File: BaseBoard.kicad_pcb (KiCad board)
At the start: 2 copper layers, 225 x 225 mm, 154 parts, among them Q1 MMBT2222A-7-F, Q10 IRLML6401TRPBF, Q11 MMBT2222A-7-F, Q12 IRLML6401TRPBF, Q13 MMBT2222A-7-F, Q14 IRLML6401TRPBF, Q15 MMBT2222A-7-F, Q16 IRLML6401TRPBF, Q2 IRLML6401TRPBF, Q3 MMBT2222A-7-F, Q4 IRLML6401TRPBF, Q5 MMBT2222A-7-F, Q6 IRLML6401TRPBF, Q7 MMBT2222A-7-F, Q8 IRLML6401TRPBF, Q9 MMBT2222A-7-F, U1 TLC5971PWPR, U10 TLC5971PWPR, U11 TLC5971PWPR, U12 TLC5971PWPR, U13 TLC5971PWPR, U14 TLC5971PWPR, U15 TLC5971PWPR, U16 TLC5971PWPR, U2 TLC5971PWPR, U3 TLC5971PWPR, U4 TLC5971PWPR, U5 TLC5971PWPR, U6 TLC5971PWPR, U7 TLC5971PWPR, U8 TLC5971PWPR, U9 TLC5971PWPR

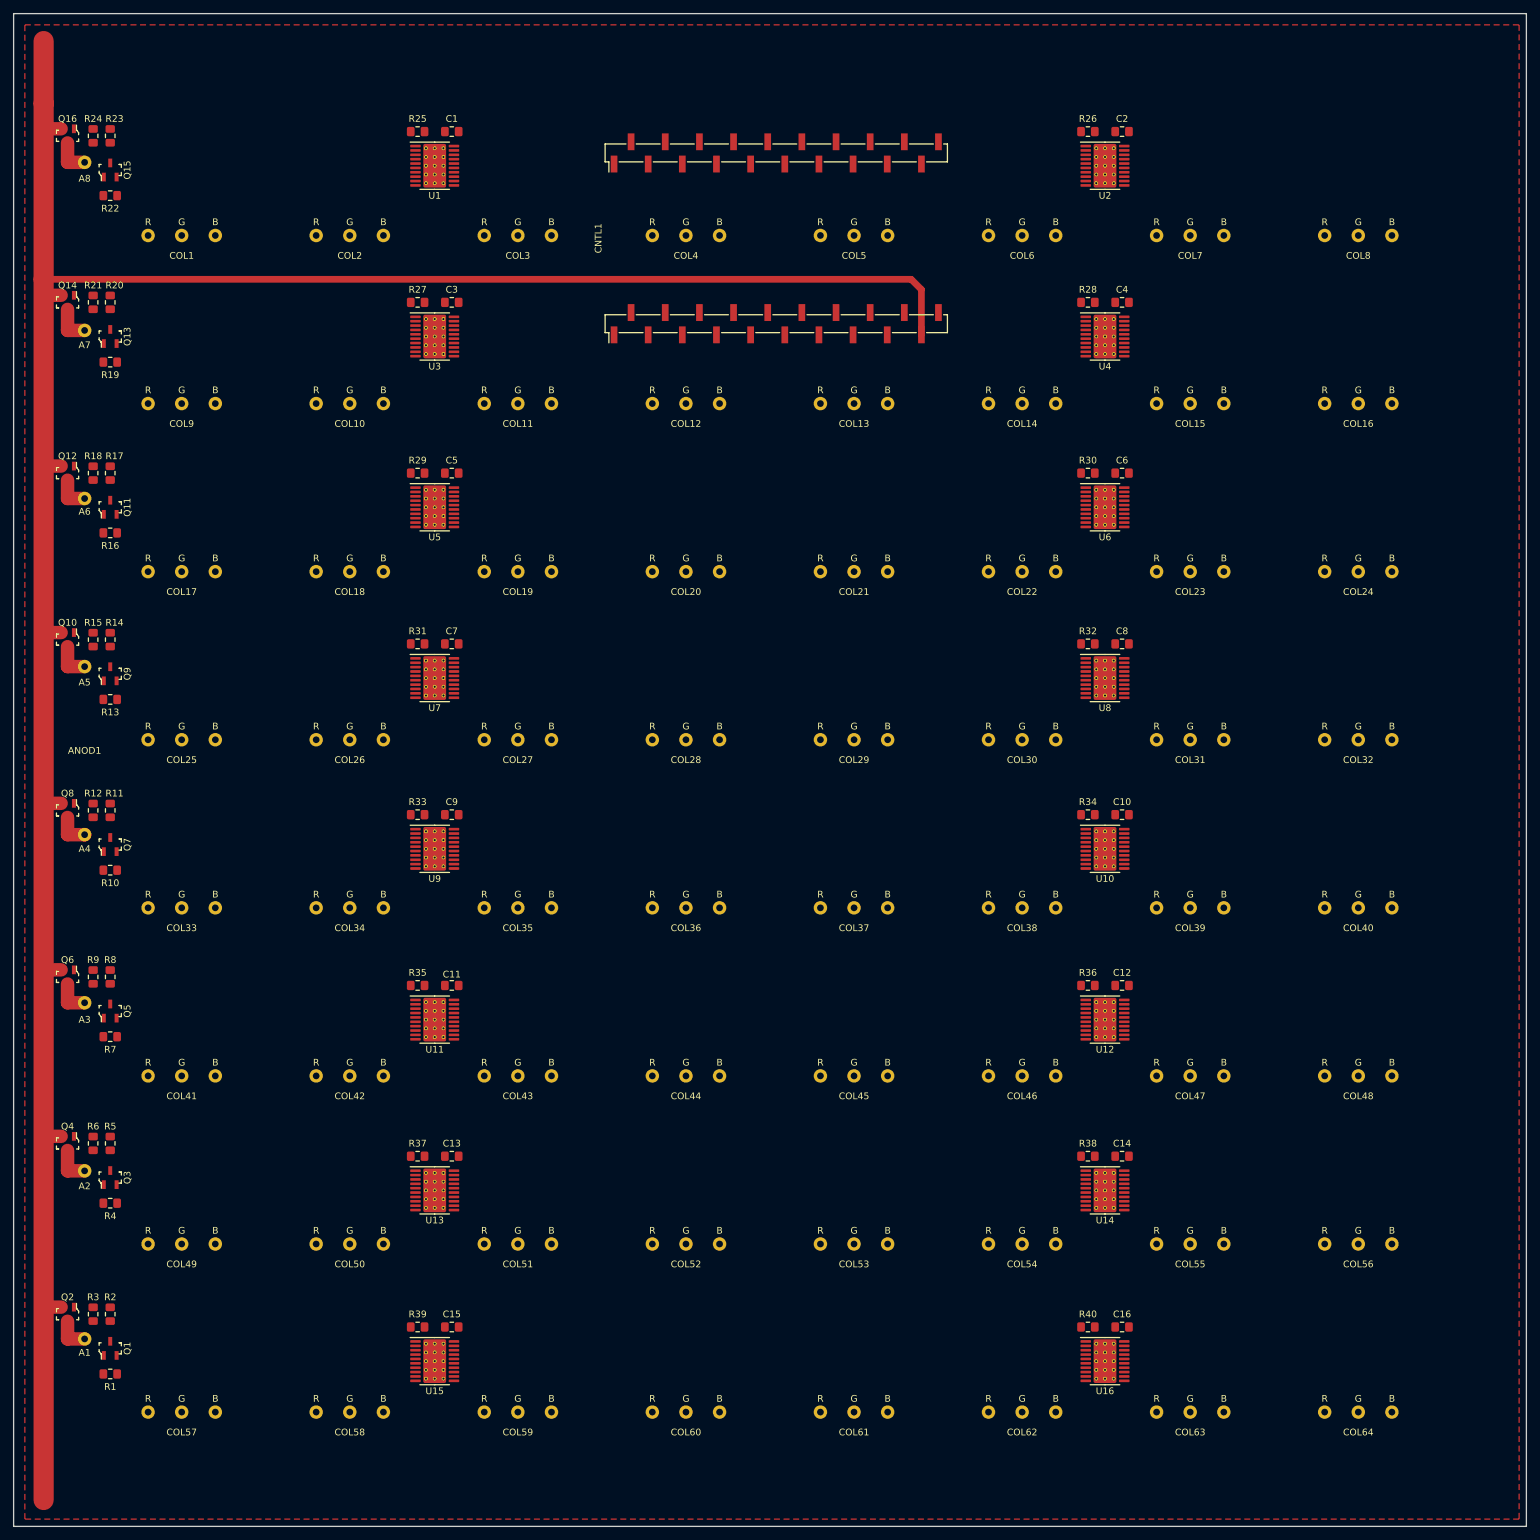
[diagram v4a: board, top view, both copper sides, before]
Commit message: Realign some components
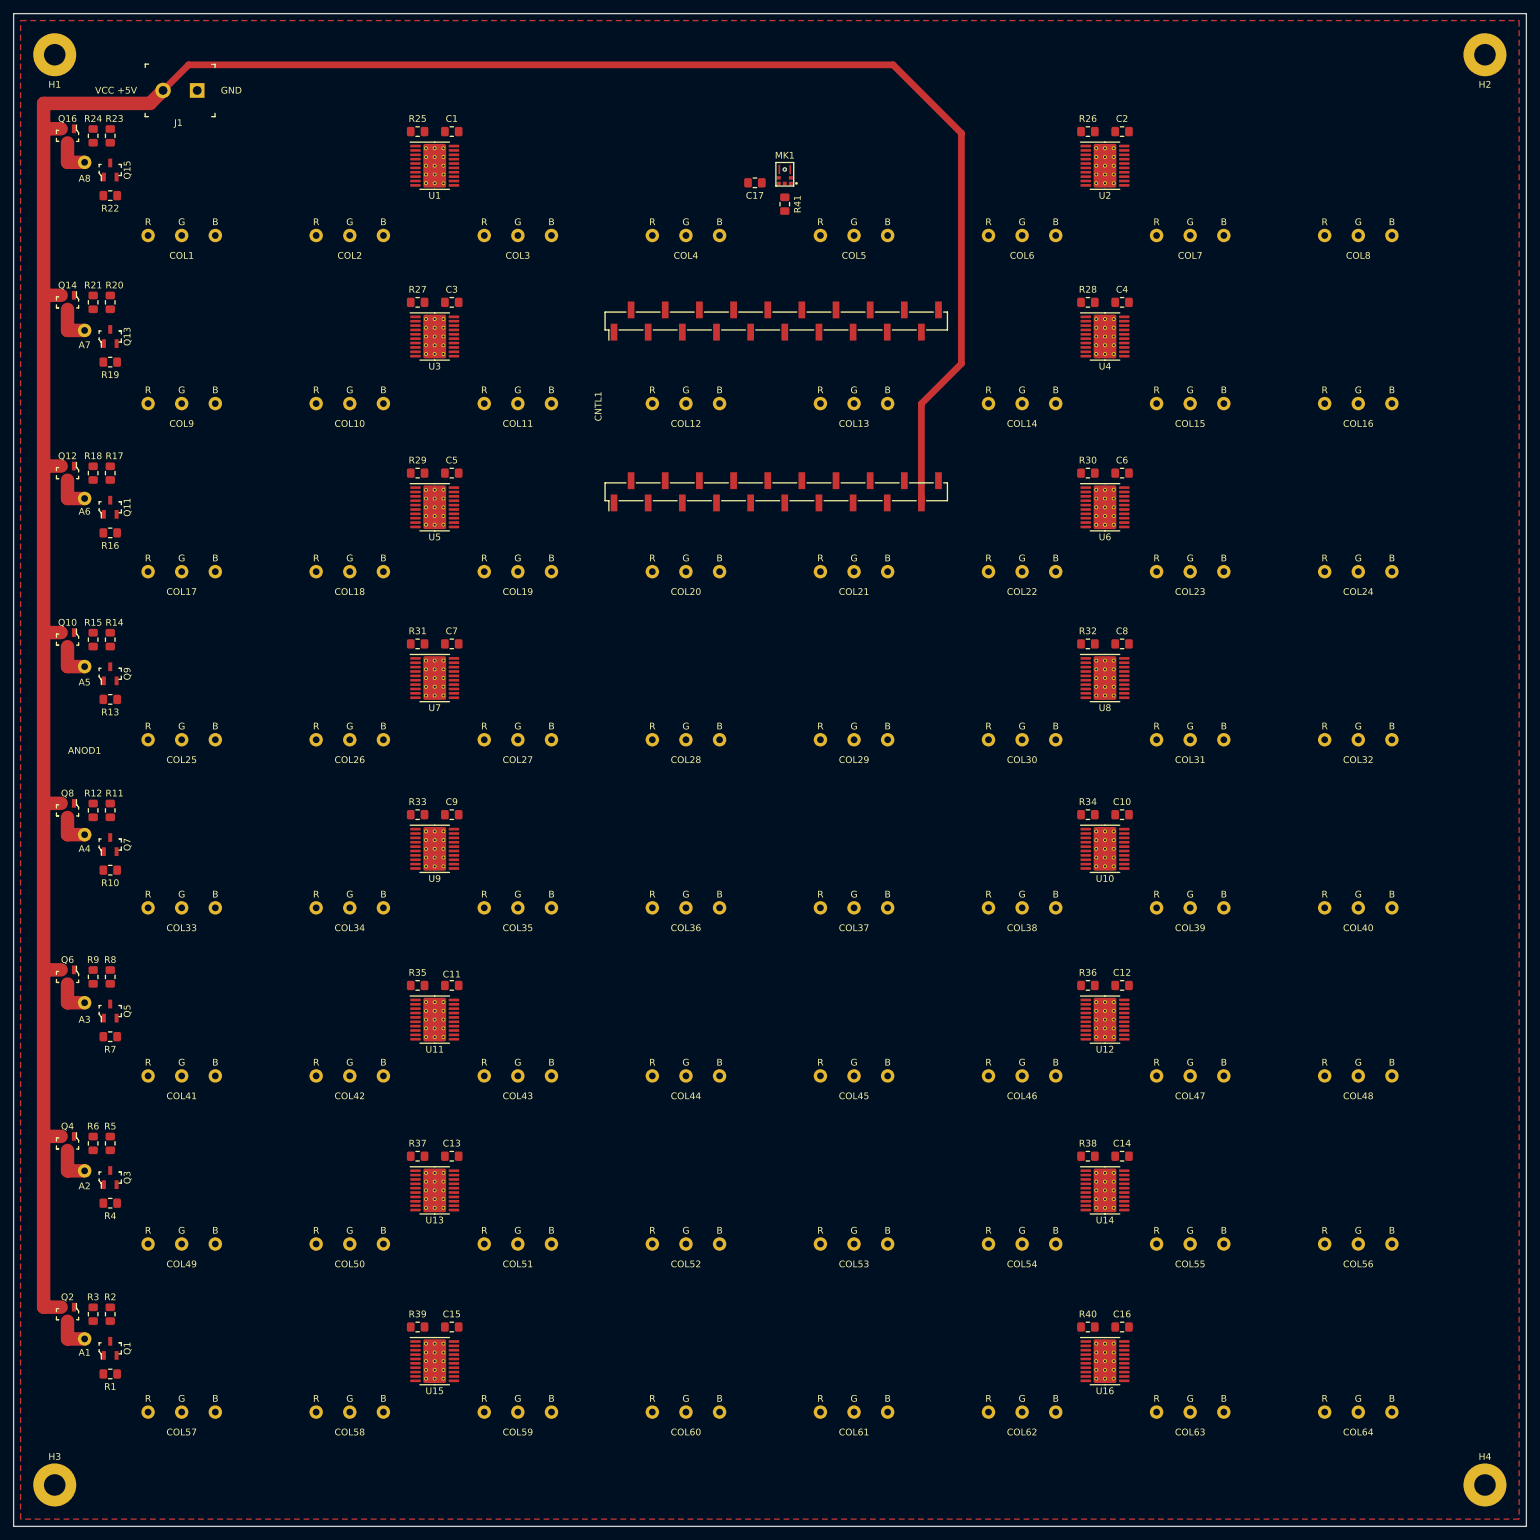
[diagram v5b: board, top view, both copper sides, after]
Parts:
- added C17: 0.1uF, Capacitor_SMD:C_0805_2012Metric_Pad1.15x1.40mm_HandSolder, F.Cu at (130.2, 45.1)
- added H1: MountingHole_3.2mm_M3_Pad, MountingHole:MountingHole_3.2mm_M3_Pad, F.Cu at (26.0, 26.0)
- added H2: MountingHole_3.2mm_M3_Pad, MountingHole:MountingHole_3.2mm_M3_Pad, F.Cu at (238.8, 26.0)
- added H3: MountingHole_3.2mm_M3_Pad, MountingHole:MountingHole_3.2mm_M3_Pad, F.Cu at (26.0, 238.8)
- added H4: MountingHole_3.2mm_M3_Pad, MountingHole:MountingHole_3.2mm_M3_Pad, F.Cu at (238.8, 238.8)
- added J1: OSTTC022162, digikey-footprints:Term_Block_1x2_P5.08MM, F.Cu at (47.2, 31.4)
- added MK1: ICS-43434, BaseBoard:MIC_ICS-43434, F.Cu at (134.6, 43.8)
- added R41: 100K, Resistor_SMD:R_0805_2012Metric_Pad1.15x1.40mm_HandSolder, F.Cu at (134.6, 48.3)
- moved CNTL1 25.0 mm to (133.3, 78.3)
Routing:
- net VCC: track 375.7 -> 400.4 mm
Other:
- board text added: "GND"
- board text added: "VCC +5V"

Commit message: Add all routing
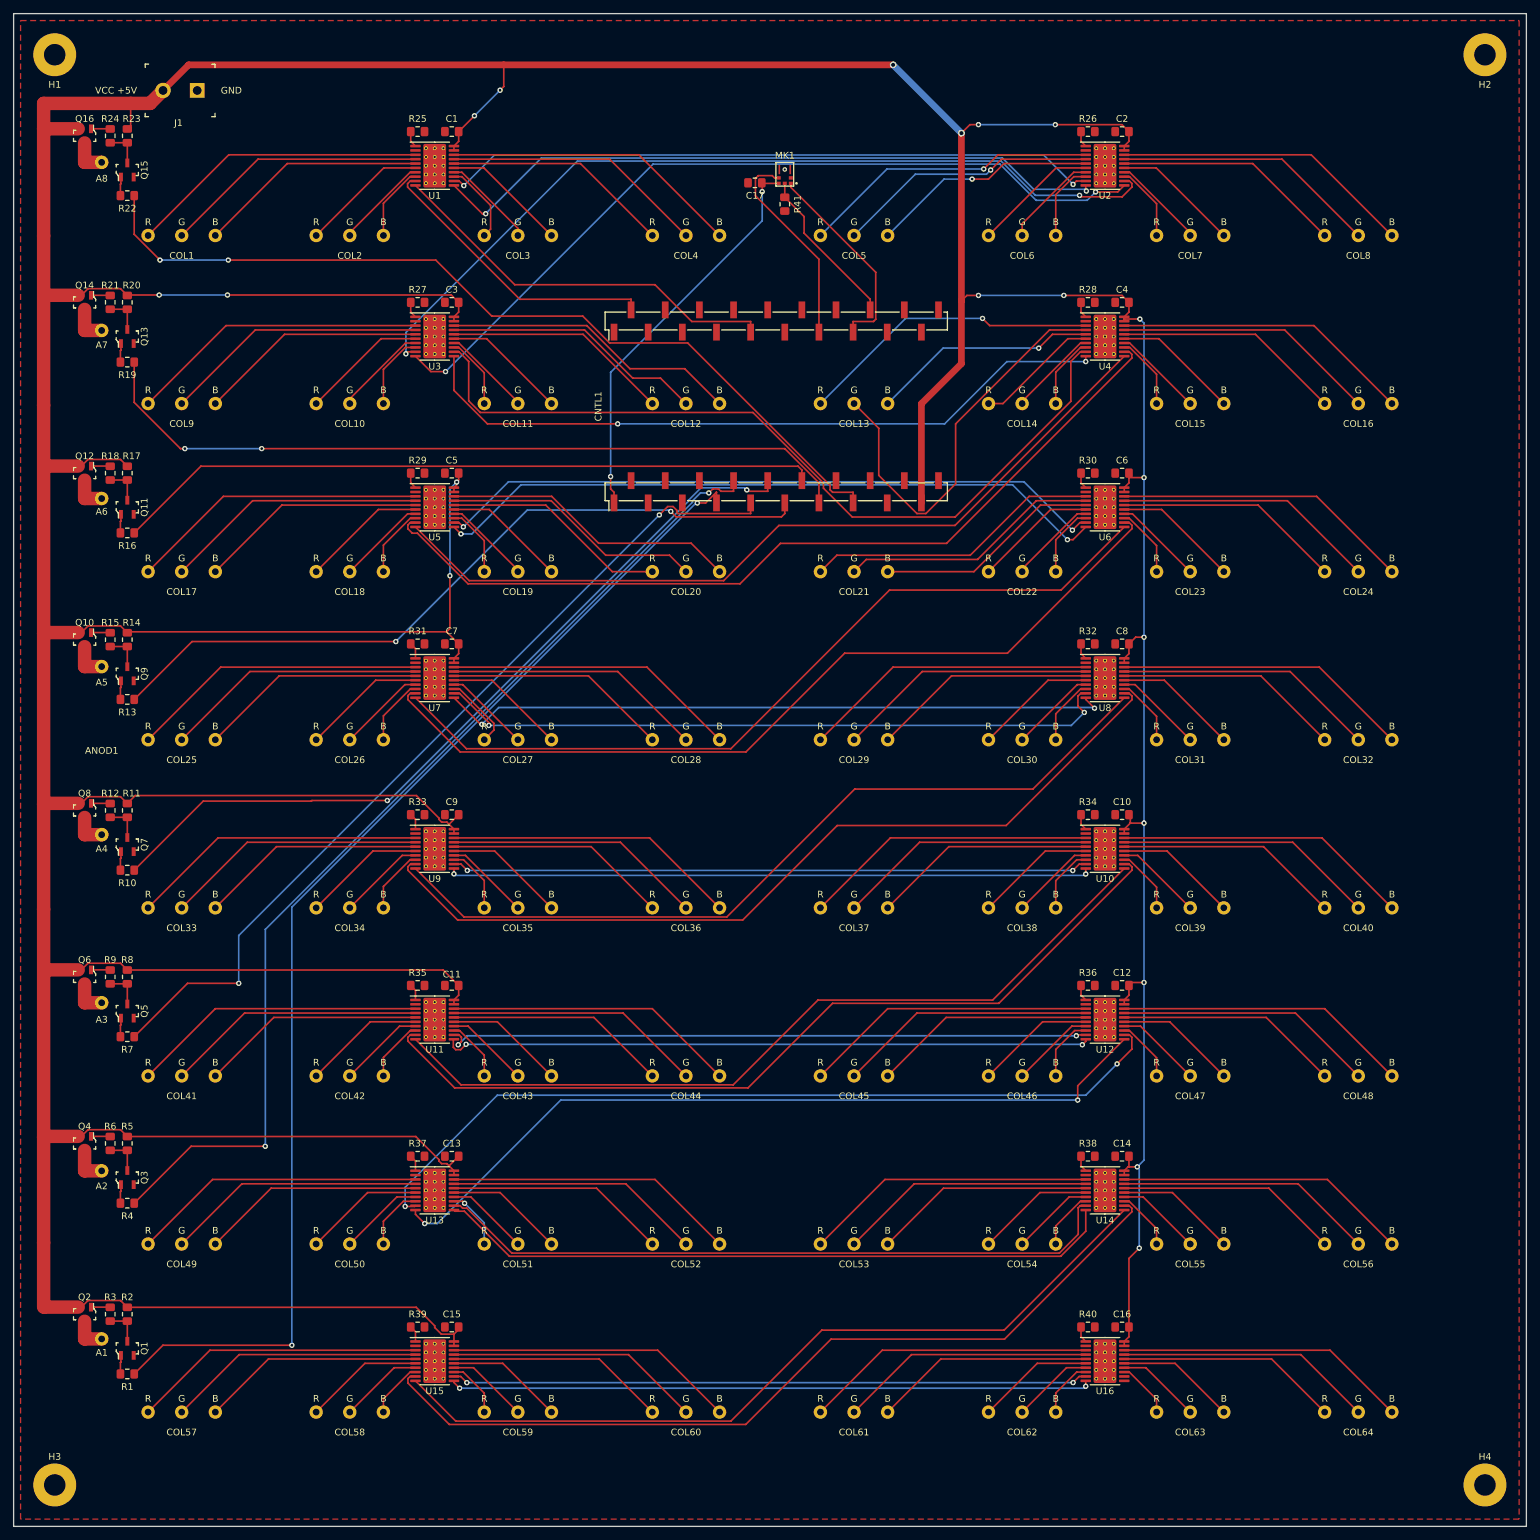
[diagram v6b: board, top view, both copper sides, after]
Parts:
- moved ANOD1 2.54 mm to (33.0, 129.5)
- moved Q1 2.54 mm to (36.8, 218.4)
- moved Q10 2.54 mm to (30.5, 113.0)
- moved Q11 2.54 mm to (36.8, 93.3)
- moved Q12 2.54 mm to (30.5, 88.3)
- moved Q13 2.54 mm to (36.8, 67.9)
- moved Q14 2.54 mm to (30.5, 62.9)
- moved Q15 2.54 mm to (36.8, 43.2)
- moved Q16 2.54 mm to (30.5, 38.1)
- moved Q2 2.54 mm to (30.5, 213.4)
- moved Q3 2.54 mm to (36.8, 193.0)
- moved Q4 2.54 mm to (30.5, 188.0)
- moved Q5 2.54 mm to (36.8, 168.3)
- moved Q6 2.54 mm to (30.5, 163.2)
- moved Q7 2.54 mm to (36.8, 143.5)
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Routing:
- net VCC: track 400.4 -> 1121.5 mm, vias 0 -> 19
- net Net-(CNTL1-Pad7): track 0.00 -> 180.7 mm, vias 0 -> 2
- net Net-(CNTL1-Pad8): track 0.00 -> 153.9 mm, vias 0 -> 2
- net Net-(CNTL1-Pad9): track 0.00 -> 130.7 mm, vias 0 -> 2
- net Net-(CNTL1-Pad15): track 0.00 -> 130.5 mm, vias 0 -> 2
- net Net-(U4-Pad12): track 0.00 -> 128.6 mm
- net Net-(U6-Pad12): track 0.00 -> 128.3 mm
- net Net-(U8-Pad12): track 0.00 -> 128.0 mm
- net Net-(U2-Pad12): track 0.00 -> 127.9 mm, vias 0 -> 2
- net Net-(U10-Pad12): track 0.00 -> 127.7 mm
- net Net-(U14-Pad12): track 0.00 -> 127.1 mm
- net Net-(U12-Pad12): track 0.00 -> 124.1 mm, vias 0 -> 2
- net Net-(U4-Pad11): track 0.00 -> 122.6 mm
- net Net-(U2-Pad11): track 0.00 -> 122.3 mm, vias 0 -> 2
- net Net-(U6-Pad11): track 0.00 -> 122.2 mm
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
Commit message: Latest changes
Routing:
- net VCC: track 1121.5 -> 1112.4 mm
- net Net-(U14-Pad11): track 120.9 -> 123.2 mm
- net Net-(U14-Pad12): track 127.1 -> 128.9 mm
- net Net-(COL51-Pad1): track 8.97 -> 9.92 mm
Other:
- rule trace_min: 0.2 -> 0.25
- board text added: "JLCJLCJLCJLC"
